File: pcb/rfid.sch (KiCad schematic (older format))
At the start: 24 parts, among them IC1 ATMEGA8-P, P1 CONN_2, P2 CONN_4, Q1 BS107, Q2 BC547, U1 LM358, X1 8MHz

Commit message: adding USB stuff to use with v-usb
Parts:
- added D? (x2): 3V6, symbol ZENER
- added J?: USB, symbol USB
- added R? (x2): 68, ~, symbol R
- added R?: 2K2, ~, symbol R
- X1: value 8MHz -> 16MHz
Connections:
- wire segments 67 -> 83

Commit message: replaced RF frontend with EM4095
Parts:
- removed C1: 1n5, ~, symbol C
- removed C2: 4n7, ~, symbol C
- removed C3: 15n, ~, symbol C
- removed D1: 1N4148, ~, symbol DIODE
- removed L1: INDUCTOR, ~, symbol INDUCTOR
- removed P1: CONN_2, symbol CONN_2
- removed P2: CONN_4, symbol CONN_4
- removed Q1: BS107, TO92, symbol BS107
- removed Q2: BC547, TO92, symbol BC547
- removed R1: 100, ~, symbol R
- removed R10: 100K, ~, symbol R
- removed R2: 1K, ~, symbol R
- removed R3: 270K, ~, symbol R
- removed R4: 4K7, ~, symbol R
- removed R5: 1K8, ~, symbol R
- removed R6, R9: 33K, ~, symbol R
- removed R7: 390K, ~, symbol R
- removed R8: 1K2, ~, symbol R
- removed U1: LM358, symbol LM358
- added C? (x5): 100n, ~, symbol C
- added C? (x3): 1n, ~, symbol C
- added C? (x3): RES, ~, symbol C
- added C? (x3): DV1, ~, symbol C
- added C?: DV2, ~, symbol C
- added C?: 4.7u, ~, symbol CP1
- added C? (x3): 100u, ~, symbol CP1
- added C?: 1u, ~, symbol C
- added D?: 5V6, ~, symbol ZENER
- added IC?: EM4095, SO16, symbol EM4095
- added L?: INDUCTOR, ~, symbol INDUCTOR
- added L?: 22uH 3A, ~, symbol INDUCTOR
- added R?: 10R, ~, symbol R
- added R?: 0R, ~, symbol R
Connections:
- net labels added: +5VA
- wire segments 83 -> 58

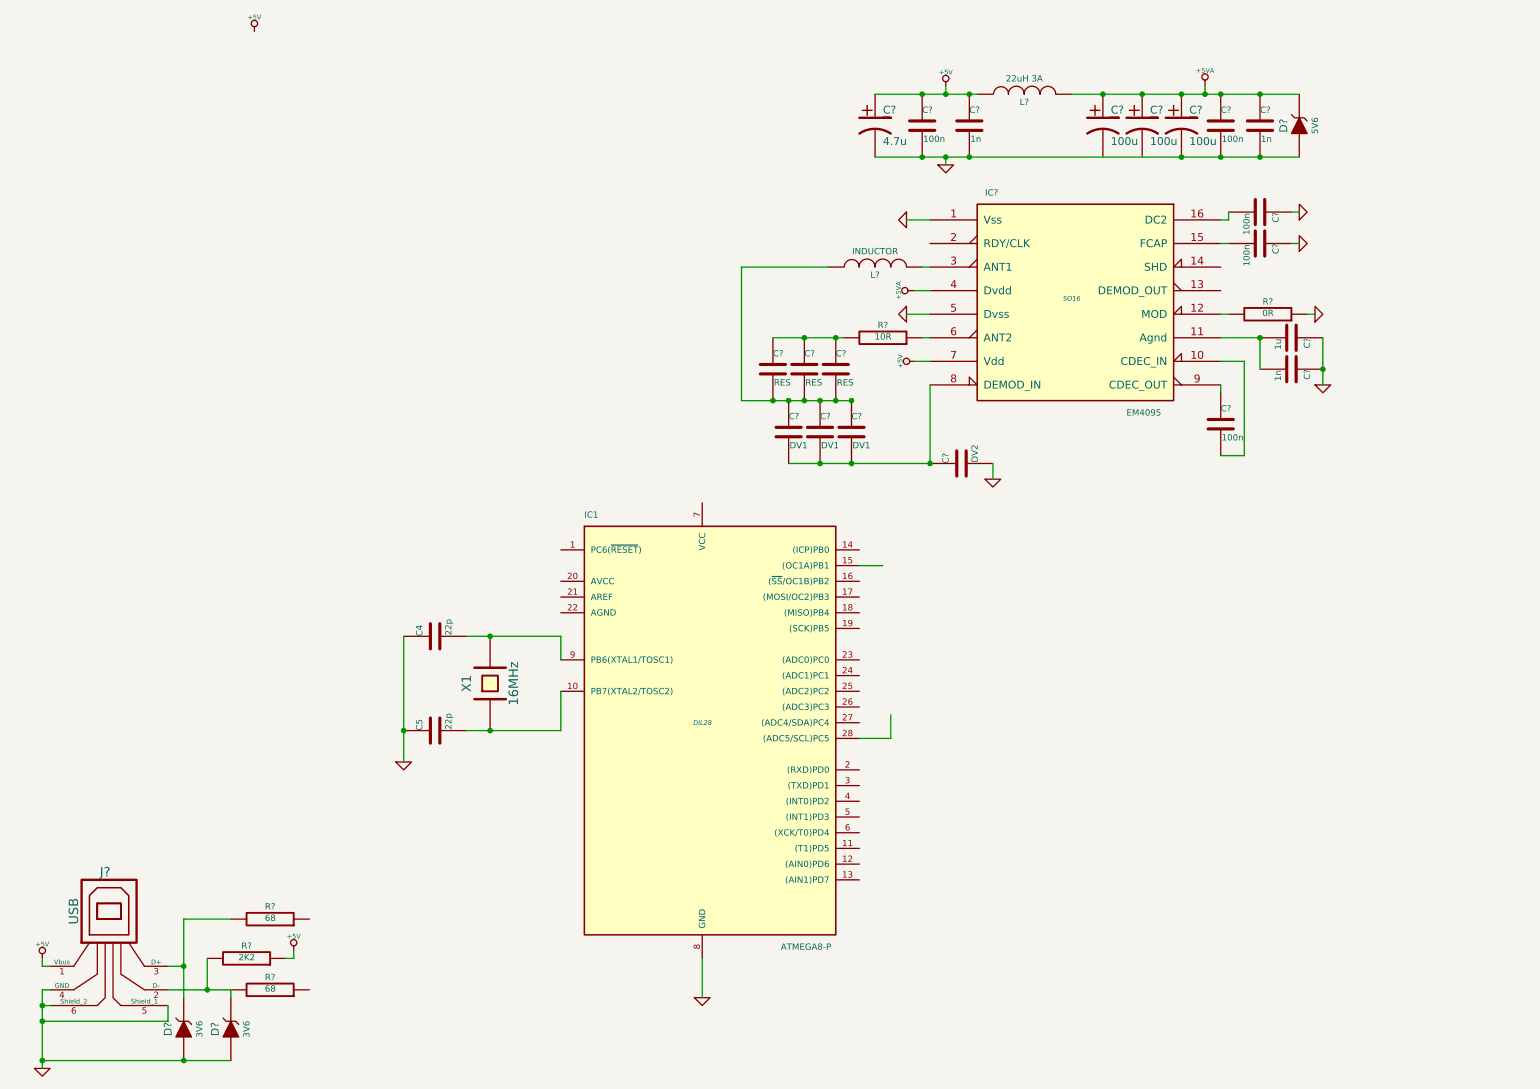
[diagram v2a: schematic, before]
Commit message: connecting attiny13 and adding schematics png
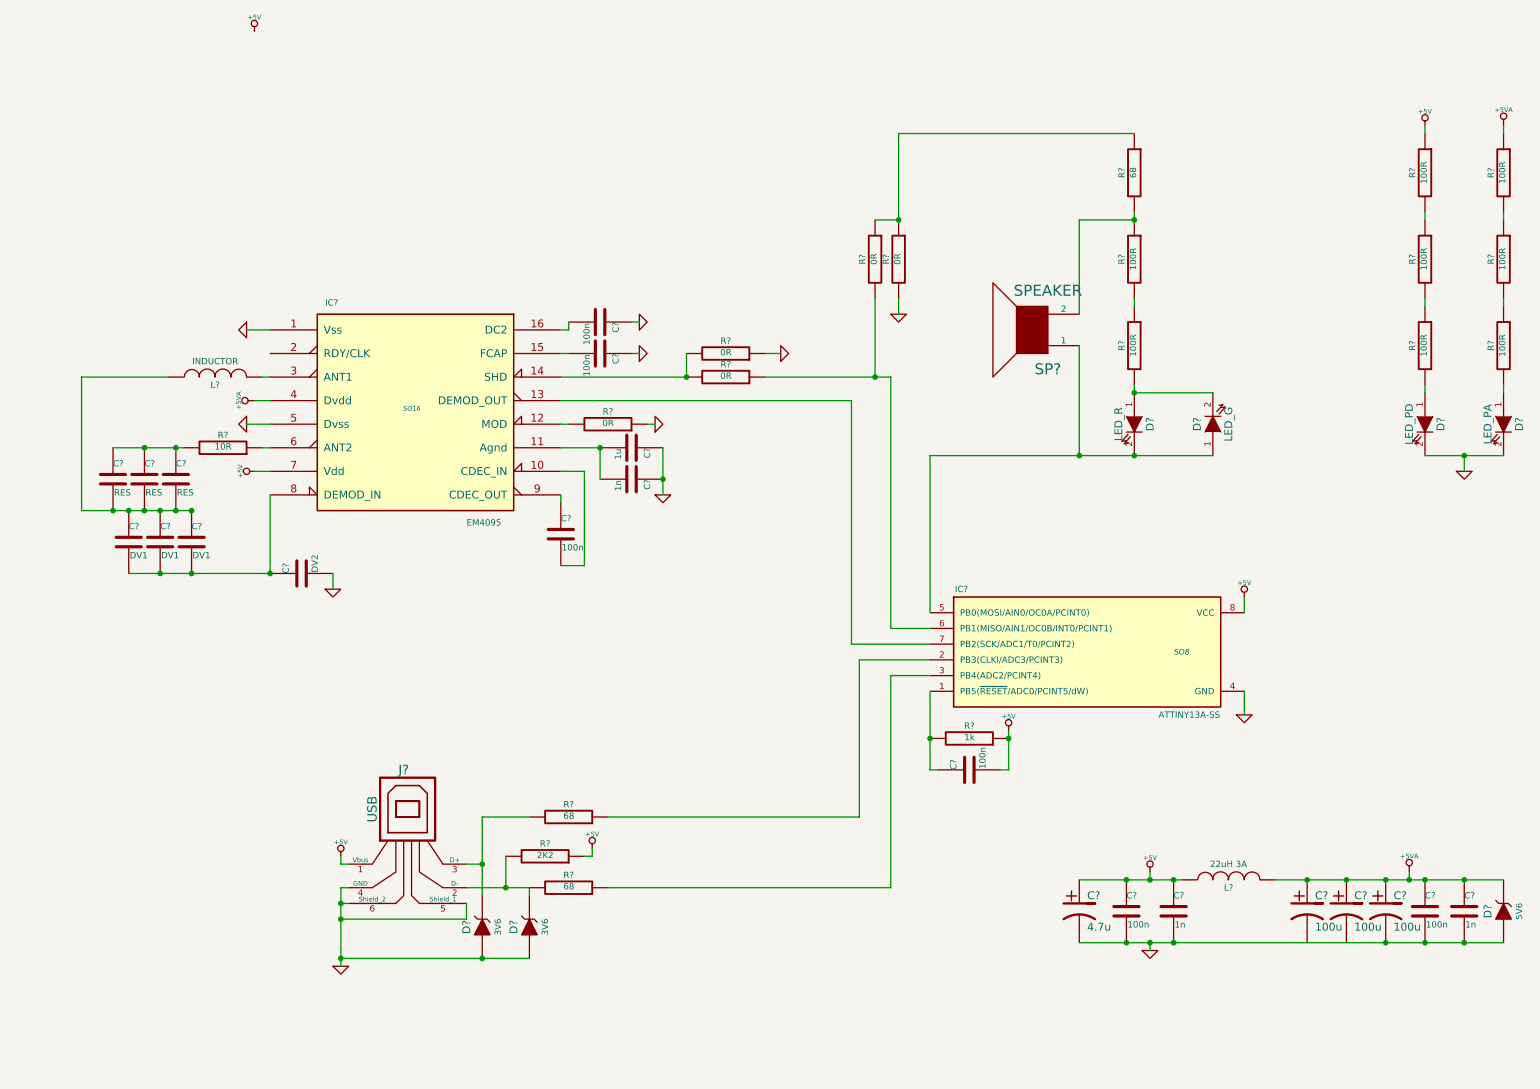
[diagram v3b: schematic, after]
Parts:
- removed C4, C5: 22p, ~, symbol C
- removed IC1: ATMEGA8-P, DIL28, symbol ATMEGA8-P
- removed X1: 16MHz, ~, symbol CRYSTAL
- added C?: 100n, ~, symbol C
- added D?: LED_PD, ~, symbol LED
- added D?: LED_PA, ~, symbol LED
- added D?: LED_R, ~, symbol LED
- added D?: LED_G, ~, symbol LED
- added IC?: ATTINY13A-SS, SO8, symbol ATTINY13A-SS
- added R? (x4): 0R, ~, symbol R
- added R?: 1k, ~, symbol R
- added R? (x8): 100R, ~, symbol R
- added R?: 68, ~, symbol R
- added SP?: SPEAKER, ~, symbol SPEAKER
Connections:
- net +5V: now also C?.2, IC?.8 (VCC), R?.1, R?.1
- net +5VA: now also R?.1
- net GND: now also D?.2 (K), D?.2 (K), IC?.4 (GND), R?.1, R?.2
- net at R?.1: now also IC?.2 (PB3(CLKI/ADC3/PCINT3))
- net at R?.1: now also IC?.3 (PB4(ADC2/PCINT4))
- net at IC?.13 (DEMOD_OUT): now also IC?.7 (PB2(SCK/ADC1/T0/PCINT2))
- net at IC?.14 (SHD): now also R?.2, R?.2
- new net: C?.1, IC?.1 (PB5(~RESET~/ADC0/PCINT5/dW)), R?.2
- new net: D?.1 (A), D?.2 (K), IC?.5 (PB0(MOSI/AIN0/OC0A/PCINT0)), SP?.1
- new net: IC?.6 (PB1(MISO/AIN1/OC0B/INT0/PCINT1)), R?.1, R?.2
- new net: D?.1 (A), R?.2 (x2)
- new net: R?.1, R?.2 (x5)
- new net: D?.1 (A), D?.2 (K), R?.2
- new net: R?.1, R?.2, SP?.2
- new net: R?.1, R?.1, R?.1
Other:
- moved on the sheet: C?, D?, IC?, J?, L?, R?

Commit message: associating footprints and minor schematics changes
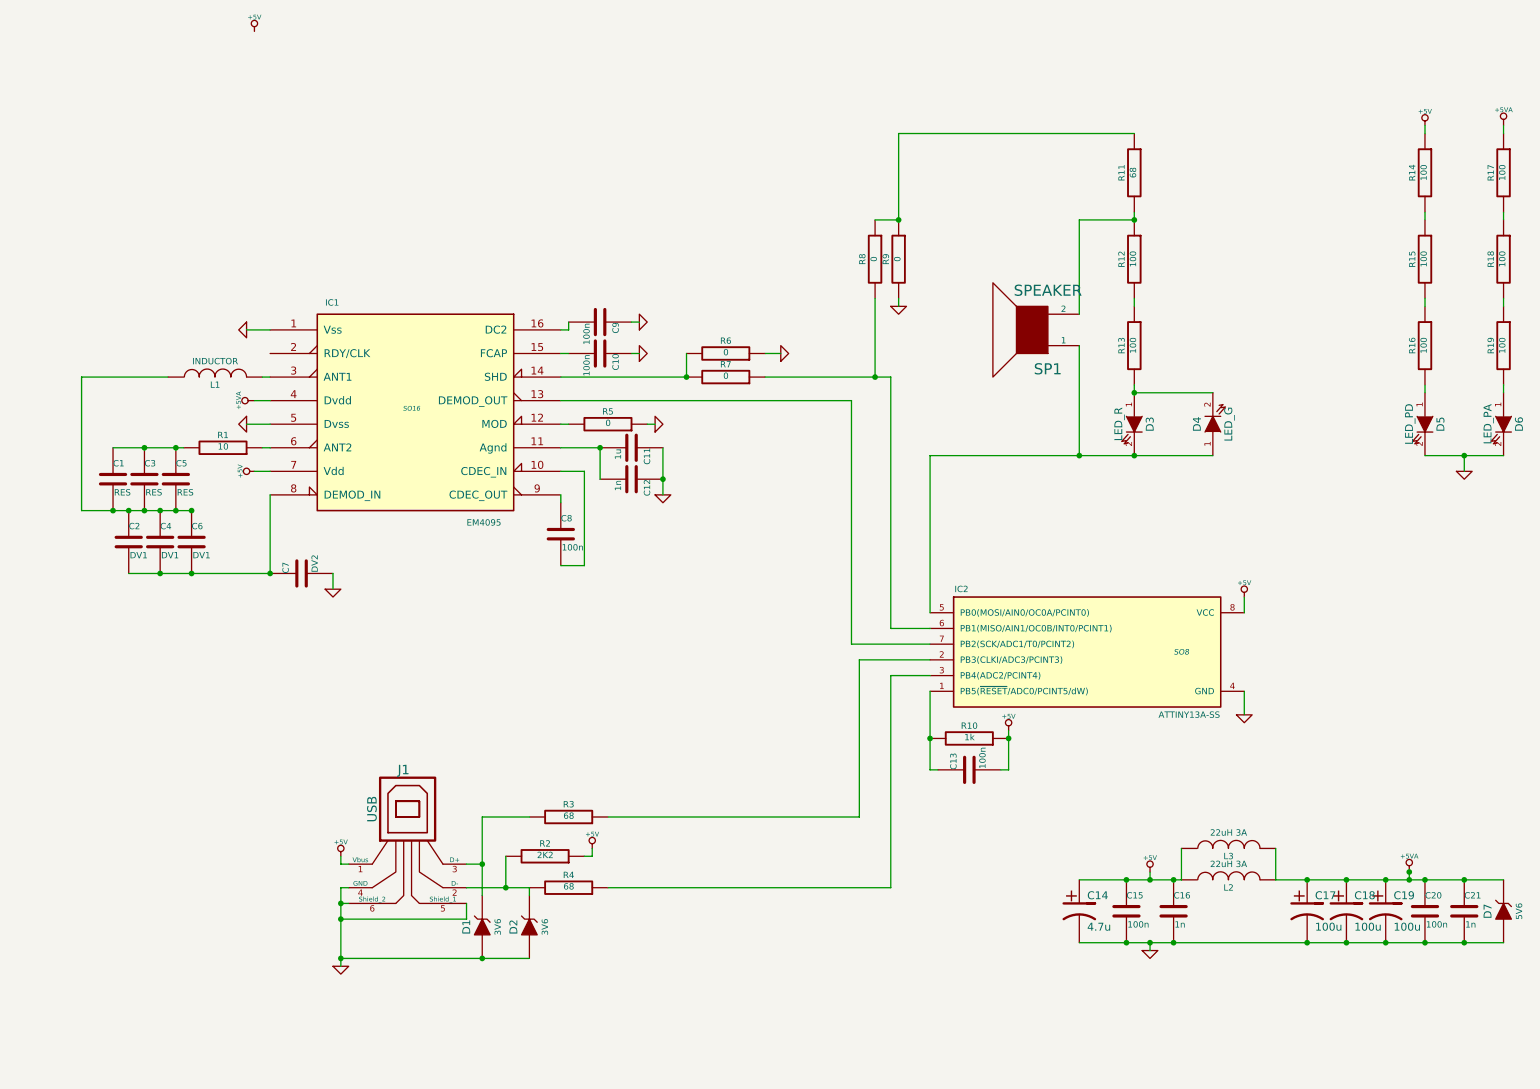
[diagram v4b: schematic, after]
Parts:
- added L3: 22uH 3A, ~, symbol INDUCTOR
- R1: renamed from R?; value 10R -> 10
- R12, R13, R14, R15, R16, R17, R18, R19: renamed from R?; value 100R -> 100
- R5, R6, R7, R8, R9: renamed from R?; value 0R -> 0
- gave numbers to parts that had none: 39
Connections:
- net +5V: now also L3.1
- net +5VA: now also L3.2
- net GND: now also C17.2, C18.2

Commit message: starting new pcb routing
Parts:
- added C22: 100n, ~, symbol C
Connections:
- net +5V: now also C22.1; no longer C13.2
- net GND: now also C13.2, C22.2
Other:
- moved on the sheet: C14
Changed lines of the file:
@@
 Sheet 1 1
 Title ""
-Date "20 sep 2014"
+Date "26 sep 2014"
 Rev ""
 Comp ""
@@
 L CP1 C14
 U 1 1 54130039
-P 7900 6150
-F 0 "C14" H 7950 6250 50  0000 L CNN
-F 1 "4.7u" H 7950 6050 50  0000 L CNN
-F 2 "~" H 7900 6150 60  0000 C CNN
-F 3 "~" H 7900 6150 60  0000 C CNN
-	1    7900 6150
+P 7550 6150
+F 0 "C14" H 7600 6250 50  0000 L CNN
+F 1 "4.7u" H 7600 6050 50  0000 L CNN
+F 2 "~" H 7550 6150 60  0000 C CNN
+F 3 "~" H 7550 6150 60  0000 C CNN
+	1    7550 6150
 	1    0    0    -1
 $EndComp
@@
 	5050 2600 5100 2600
 Wire Wire Line
-	7900 5950 8550 5950
-Wire Wire Line
-	7900 6350 10600 6350
+	7550 5950 8550 5950
+Wire Wire Line
+	7550 6350 10600 6350
 Wire Wire Line
 	8350 6400 8350 6350
@@
 	8950 4250 8950 4150
 Wire Wire Line
-	7450 5000 7450 5250
-Wire Wire Line
 	6950 4750 6950 5250
 Wire Wire Line
@@
 Connection ~ 6950 5050
 Wire Wire Line
-	7450 5250 7400 5250
-Connection ~ 7450 5050
-Wire Wire Line
 	8250 1200 6750 1200
 Wire Wire Line
@@
 Wire Wire Line
 	8550 5950 8550 5750
+$Comp
+L GND #PWR025
+U 1 1 54255A0A
+P 7450 5350
+F 0 "#PWR025" H 7450 5350 30  0001 C CNN
+F 1 "GND" H 7450 5280 30  0001 C CNN
+F 2 "" H 7450 5350 60  0001 C CNN
+F 3 "" H 7450 5350 60  0001 C CNN
+	1    7450 5350
+	1    0    0    -1
+$EndComp
+Wire Wire Line
+	7400 5250 7450 5250
+Wire Wire Line
+	7450 5250 7450 5350
+Wire Wire Line
+	7450 5050 7450 5000
+$Comp
+L C C22
+U 1 1 54255D02
+P 7900 6150
+F 0 "C22" H 7900 6250 40  0000 L CNN
+F 1 "100n" H 7906 6065 40  0000 L CNN
+F 2 "~" H 7938 6000 30  0000 C CNN
+F 3 "~" H 7900 6150 60  0000 C CNN
+	1    7900 6150
+	1    0    0    -1
+$EndComp
+Connection ~ 7900 5950
+Connection ~ 7900 6350
 $EndSCHEMATC

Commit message: adding ISP pads to schematics
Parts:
- added P1, P2, P3, P4, P5, P6: CONN_1, symbol CONN_1
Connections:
- net labels added: MISO, MOSI, RST, SCK
- wire segments 97 -> 113
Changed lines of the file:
@@
 Sheet 1 1
 Title ""
-Date "26 sep 2014"
+Date "14 oct 2014"
 Rev ""
 Comp ""
@@
 $EndComp
 Wire Wire Line
-	6950 4450 6450 4450
+	6150 4450 6950 4450
 Wire Wire Line
 	6450 4450 6450 2900
@@
 	6700 2750 6700 4350
 Wire Wire Line
-	6700 4350 6950 4350
+	6100 4350 6950 4350
 Wire Wire Line
 	5900 2600 6000 2600
@@
 Connection ~ 7900 5950
 Connection ~ 7900 6350
+Wire Wire Line
+	6100 4350 6100 4200
+Wire Wire Line
+	6100 4200 5950 4200
+Connection ~ 6700 4350
+Wire Wire Line
+	6150 4450 6150 4150
+Wire Wire Line
+	6150 4150 5850 4150
+Wire Wire Line
+	5850 4150 5850 4200
+Connection ~ 6450 4450
+Wire Wire Line
+	6950 4750 6200 4750
+Wire Wire Line
+	6200 4750 6200 4100
+Wire Wire Line
+	6200 4100 5750 4100
+Wire Wire Line
+	5750 4100 5750 4200
+Wire Wire Line
+	6950 4250 6250 4250
+Wire Wire Line
+	6250 4250 6250 5050
+Wire Wire Line
+	6250 5050 5850 5050
+Wire Wire Line
+	5850 5050 5850 5000
+$Comp
+L GND #PWR026
+U 1 1 543D6888
+P 5750 5150
+F 0 "#PWR026" H 5750 5150 30  0001 C CNN
+F 1 "GND" H 5750 5080 30  0001 C CNN
+F 2 "" H 5750 5150 60  0001 C CNN
+F 3 "" H 5750 5150 60  0001 C CNN
+	1    5750 5150
+	1    0    0    -1
+$EndComp
+Wire Wire Line
+	5750 5000 5750 5150
+Wire Wire Line
+	5950 5000 6100 5000
+Wire Wire Line
+	6100 5000 6100 4900
+$Comp
+L +5V #PWR027
+U 1 1 543D69D3
+P 6100 4900
+F 0 "#PWR027" H 6100 4990 20  0001 C CNN
+F 1 "+5V" H 6100 4990 30  0000 C CNN
+F 2 "" H 6100 4900 60  0001 C CNN
+F 3 "" H 6100 4900 60  0001 C CNN
+	1    6100 4900
+	1    0    0    -1
+$EndComp
+Text Label 6950 3850 0    60   ~ 0
+MOSI
+Text Label 6700 4000 0    60   ~ 0
+MISO
+Text Label 6450 4050 0    60   ~ 0
+SCK
+Text Label 6300 4750 0    60   ~ 0
+RST
+$Comp
+L CONN_1 P5
+U 1 1 543D6CCD
+P 5950 4350
+F 0 "P5" H 6030 4350 40  0000 L CNN
+F 1 "CONN_1" H 5950 4405 30  0001 C CNN
+F 2 "" H 5950 4350 60  0000 C CNN
+F 3 "" H 5950 4350 60  0000 C CNN
+	1    5950 4350
+	0    1    1    0
+$EndComp
+$Comp
+L CONN_1 P6
+U 1 1 543D6CDC
+P 5950 4850
+F 0 "P6" H 6030 4850 40  0000 L CNN
+F 1 "CONN_1" H 5950 4905 30  0001 C CNN
+F 2 "" H 5950 4850 60  0000 C CNN
+F 3 "" H 5950 4850 60  0000 C CNN
+	1    5950 4850
+	0    -1   -1   0
+$EndComp
+$Comp
+L CONN_1 P3
+U 1 1 543D6CEB
+P 5850 4350
+F 0 "P3" H 5930 4350 40  0000 L CNN
+F 1 "CONN_1" H 5850 4405 30  0001 C CNN
+F 2 "" H 5850 4350 60  0000 C CNN
+F 3 "" H 5850 4350 60  0000 C CNN
+	1    5850 4350
+	0    1    1    0
+$EndComp
+$Comp
+L CONN_1 P4
+U 1 1 543D6CFA
+P 5850 4850
+F 0 "P4" H 5930 4850 40  0000 L CNN
+F 1 "CONN_1" H 5850 4905 30  0001 C CNN
+F 2 "" H 5850 4850 60  0000 C CNN
+F 3 "" H 5850 4850 60  0000 C CNN
+	1    5850 4850
+	0    -1   -1   0
+$EndComp
+$Comp
+L CONN_1 P1
+U 1 1 543D6D09
+P 5750 4350
+F 0 "P1" H 5830 4350 40  0000 L CNN
+F 1 "CONN_1" H 5750 4405 30  0001 C CNN
+F 2 "" H 5750 4350 60  0000 C CNN
+F 3 "" H 5750 4350 60  0000 C CNN
+	1    5750 4350
+	0    1    1    0
+$EndComp
+$Comp
+L CONN_1 P2
+U 1 1 543D6D22
+P 5750 4850
+F 0 "P2" H 5830 4850 40  0000 L CNN
+F 1 "CONN_1" H 5750 4905 30  0001 C CNN
+F 2 "" H 5750 4850 60  0000 C CNN
+F 3 "" H 5750 4850 60  0000 C CNN
+	1    5750 4850
+	0    -1   -1   0
+$EndComp
 $EndSCHEMATC
